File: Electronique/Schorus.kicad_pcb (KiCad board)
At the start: 2 copper layers, 100 x 100 mm, 87 parts, among them J1 Coaxial connector 2.1mm, J2 1/4 inch jack, J3 1/4 inch jack, Q1 BC548, Q2 BF245C, Q3 BC548, SW1 3PDT, SW2 SPDT, SW3 SPDT, SW4 DPDT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

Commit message: Placement des empreintes.
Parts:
- added REF**: PinHeader_1x03_P2.54mm_Vertical, Connector_PinHeader_2.54mm:PinHeader_1x03_P2.54mm_Vertical, F.Cu at (92.7, 67.3)
- moved R33 208.7 mm to (22.9, 97.8), turned to 90 degrees
- moved R35 197.3 mm to (19.1, 97.8), turned to 90 degrees
- moved R6 149.1 mm to (101.6, 50.8), turned to 270 degrees
- moved R9 148.6 mm to (110.5, 71.1), turned to 0 degrees
- moved R12 140.2 mm to (104.1, 34.3), turned to 90 degrees
- moved C6 134.4 mm to (110.5, 57.1), turned to 0 degrees
- moved R11 133.1 mm to (97.8, 50.8), turned to 270 degrees
- moved R16 130.9 mm to (120.7, 67.3), turned to 180 degrees
- moved J1 119.3 mm to (82.5, 85.1), turned to 180 degrees
- moved Q2 112.4 mm to (97.8, 67.3), turned to 270 degrees
- moved R22 110.6 mm to (116.8, 59.7), turned to 0 degrees
- moved D2 105.1 mm to (108.0, 34.3), turned to 90 degrees
- moved R15 104.0 mm to (111.8, 34.3), turned to 90 degrees
- moved U3 103.5 mm to (120.7, 43.2), turned to 270 degrees
- moved C4 97.1 mm to (120.7, 54.6), turned to 0 degrees
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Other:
- board size 100 x 100 mm -> 114.8 x 86 mm
- board text added: "G S D"
- board text added: "OAM SCHÖRUS"

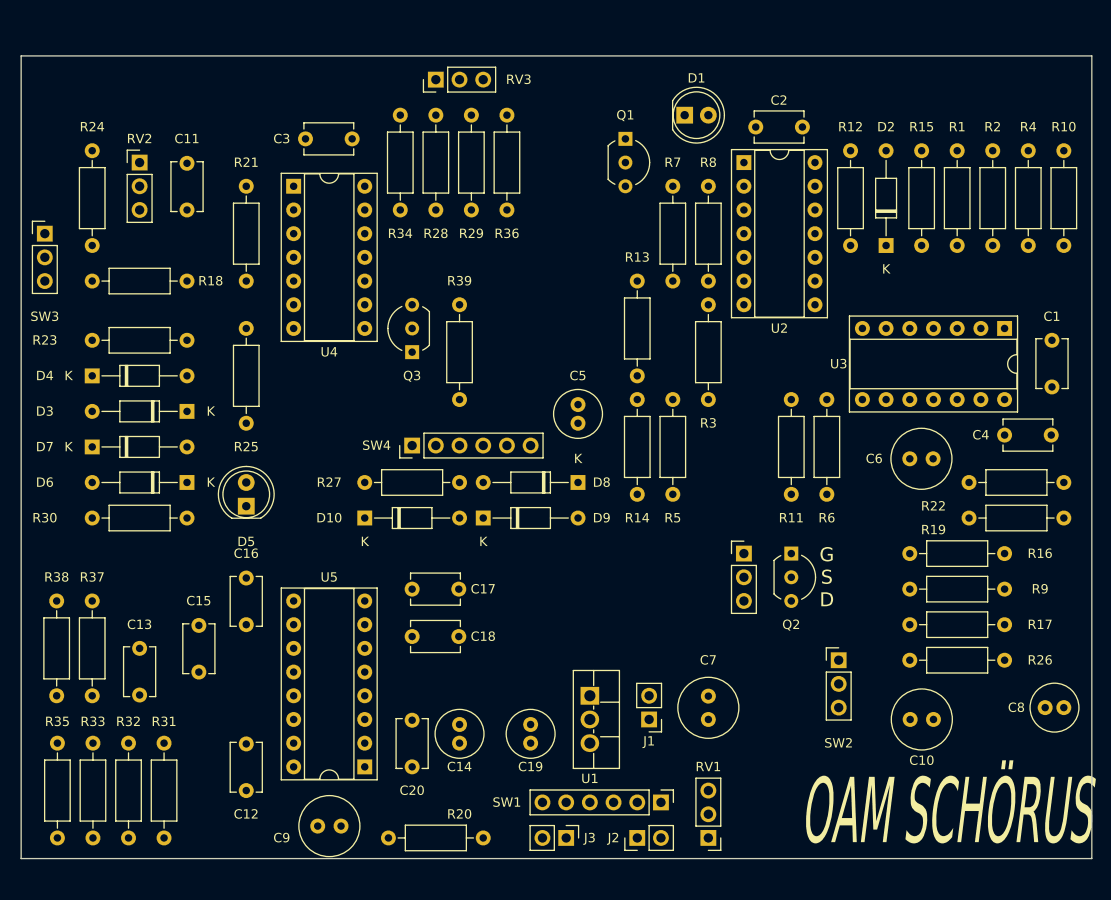
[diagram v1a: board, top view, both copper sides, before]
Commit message: Circuit imprimé en attente d'être imprimé par un professionnel.
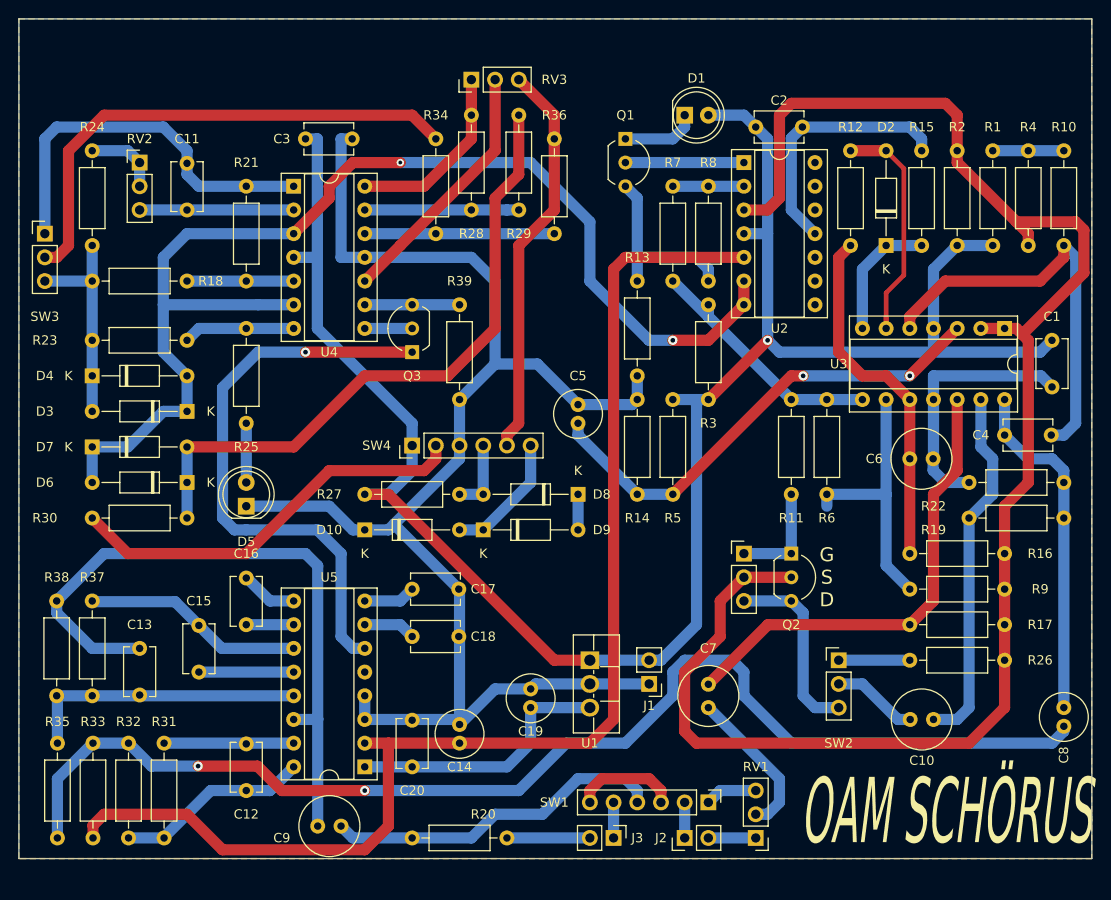
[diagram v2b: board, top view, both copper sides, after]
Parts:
- moved R36 5.68 mm to (72.4, 22.9)
- moved SW1 5.08 mm to (88.9, 94.0)
- moved J2 5.08 mm to (86.4, 97.8)
- moved J3 5.08 mm to (78.7, 97.8)
- moved R29 5.08 mm to (68.6, 20.3)
- moved RV1 5.08 mm to (94.0, 97.8)
- moved R34 4.58 mm to (59.7, 22.9)
- moved C19 3.81 mm to (69.8, 83.8)
- moved J1 3.81 mm to (82.5, 81.3)
- moved R1 3.81 mm to (119.4, 24.1)
- moved R2 3.81 mm to (115.6, 24.1)
- moved R28 3.81 mm to (63.5, 30.5)
- moved RV3 3.81 mm to (63.5, 16.5)
- moved U1 3.81 mm to (76.2, 78.7)
- moved R20 2.54 mm to (67.3, 97.8)
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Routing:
- net GND: track 0.00 -> 227.6 mm
- net +9V: track 0.00 -> 210.5 mm, vias 0 -> 1
- net VCOM: track 0.00 -> 178.6 mm
- net Net-(C14-Pad1): track 0.00 -> 135.5 mm
- net Net-(C8-Pad2): track 0.00 -> 131.4 mm, vias 0 -> 2
- net /REF: track 0.00 -> 130.0 mm, vias 0 -> 2
- net Net-(C13-Pad1): track 0.00 -> 72.9 mm
- net Net-(D6-Pad1): track 0.00 -> 69.8 mm
- net Net-(Q3-Pad1): track 0.00 -> 62.1 mm, vias 0 -> 1
- net Net-(R34-Pad1): track 0.00 -> 55.2 mm
- net Net-(C5-Pad1): track 0.00 -> 51.7 mm, vias 0 -> 2
- net Net-(C7-Pad2): track 0.00 -> 50.5 mm
- net Net-(C4-Pad2): track 0.00 -> 44.4 mm
- net Net-(R30-Pad1): track 0.00 -> 44.0 mm
- net Net-(R36-Pad1): track 0.00 -> 42.9 mm
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- added copper zone on B.Cu, net GND
- added copper zone on F.Cu, net GND
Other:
- board size 114.8 x 86 mm -> 115 x 90 mm

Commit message: Logo sur le circuit imprimé
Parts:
- moved D5 5.00 mm to (39.4, 67.2)
- moved C1 5.00 mm to (125.7, 49.5)
- moved C10 5.00 mm to (113.0, 90.1)
- moved C12 5.00 mm to (39.4, 97.7)
- moved C13 5.00 mm to (27.9, 82.5)
- moved C14 5.00 mm to (62.2, 92.6)
- moved C15 5.00 mm to (34.3, 85.0)
- moved C16 5.00 mm to (39.4, 79.9)
- moved C17 5.00 mm to (57.1, 76.1)
- moved C18 5.00 mm to (57.1, 81.2)
- moved C19 5.00 mm to (69.8, 88.8)
- moved C2 5.00 mm to (94.0, 26.6)
- moved C20 5.00 mm to (57.1, 95.2)
- moved C3 5.00 mm to (45.7, 27.9)
- moved C4 5.00 mm to (120.7, 59.6)
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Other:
- net class Default: via_dia 0.8 -> 0.6; via_drill 0.4 -> 0.35
- rule via_min_drill: 0.3 -> 0.35
- rule via_min_size: 0.4 -> 0.6
